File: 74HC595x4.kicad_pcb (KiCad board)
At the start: 2 copper layers, 45 parts, among them P1 CONN_01X06, P2 CONN_02X08, P3 CONN_02X08, P4 CONN_02X08, P5 CONN_02X08, U1 74HC595, U2 74HC595, U3 74HC595, U4 74HC595

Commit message: расставлено по сетке, исправлены ошибки
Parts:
- added C1: C, Capacitors_SMD:C_0805_HandSoldering, F.Cu at (104.1, 88.6)
- added C2: C, Capacitors_SMD:C_0805_HandSoldering, F.Cu at (104.1, 113.0)
- added C3: C, Capacitors_SMD:C_0805_HandSoldering, F.Cu at (132.1, 88.6)
- added C4: C, Capacitors_SMD:C_0805_HandSoldering, F.Cu at (132.1, 113.0)
- moved R27 51.3 mm to (139.7, 105.4)
- moved R29 51.3 mm to (147.3, 105.4)
- moved R17 51.3 mm to (121.9, 105.4)
- moved R19 51.3 mm to (111.8, 105.4)
- moved R22 51.3 mm to (114.3, 105.4)
- moved R24 51.3 mm to (104.1, 105.4)
- moved R18 51.3 mm to (116.8, 105.4)
- moved R20 51.3 mm to (106.7, 105.4)
- moved R21 51.3 mm to (119.4, 105.4)
- moved R23 51.3 mm to (109.2, 105.4)
- moved R25 51.3 mm to (149.9, 105.4)
- moved R26 51.3 mm to (144.8, 105.4)
- moved R28 51.3 mm to (134.6, 105.4)
- moved R30 51.3 mm to (142.2, 105.4)
- moved R31 51.3 mm to (137.2, 105.4)
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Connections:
- U2 pad 11: /74HC595_1/DS -> /74HC595_1/SH_CP
- U2 pad 12: /74HC595_1/SH_CP -> /74HC595_1/ST_CP
- U3 pad 11: /74HC595_1/DS -> /74HC595_1/SH_CP
- U3 pad 12: /74HC595_1/SH_CP -> /74HC595_1/ST_CP
- U4 pad 11: /74HC595_1/DS -> /74HC595_1/SH_CP
- U4 pad 12: /74HC595_1/SH_CP -> /74HC595_1/ST_CP
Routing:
- net GND: track 205.5 -> 19.9 mm, vias 0 -> 10
- net VCC: track 0.00 -> 131.4 mm, vias 0 -> 6
- net /74HC595_1/ST_CP: track 0.00 -> 107.9 mm, vias 0 -> 2
- net /74HC595_1/SH_CP: track 0.00 -> 99.8 mm, vias 0 -> 6
- net /74HC595_3/DS: track 0.00 -> 42.6 mm, vias 0 -> 2
- net /74HC595_2/DS: track 0.00 -> 40.7 mm, vias 0 -> 2
- net /74HC595_4/DS: track 0.00 -> 40.0 mm
- net /74HC595_1/DS: track 0.00 -> 19.1 mm, vias 0 -> 1
- net Net-(R29-Pad2): track 7.12 -> 5.01 mm
- net Net-(R26-Pad2): track 6.00 -> 3.88 mm
- net Net-(R10-Pad2): track 5.85 -> 3.88 mm
- net Net-(R2-Pad2): track 5.81 -> 3.88 mm
- net Net-(R18-Pad2): track 5.78 -> 3.88 mm
- net Net-(R5-Pad2): track 6.49 -> 5.01 mm
- net Net-(R13-Pad2): track 6.53 -> 5.15 mm
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
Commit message: пред готовность. толстые питающие метрические размеры
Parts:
- moved REF** 3.47 mm to (96.0, 119.0)
- moved REF** 3.44 mm to (156.0, 119.0)
- moved REF** 1.07 mm to (96.0, 74.0)
- moved REF** 0.95 mm to (156.0, 74.0)
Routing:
- net /74HC595_4/~Q7: track 0.00 -> 49.5 mm, vias 0 -> 1
- net VCC: track 131.4 -> 139.7 mm, vias 6 -> 8
- net GND: track 19.9 -> 24.4 mm, vias 10 -> 9
- net /74HC595_1/SH_CP: track 99.8 -> 103.1 mm, vias 6 -> 5
- net /74HC595_4/DS: track 40.0 -> 41.3 mm
- net /74HC595_1/ST_CP: track 107.9 -> 106.9 mm
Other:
- board outline added: 70 x 55 mm
- net class power added: clearance 0.2, trace_width 0.5, via_dia 0.6, via_drill 0.4

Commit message: мелкие доделки переразвод
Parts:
- moved REF** 10.0 mm to (96.0, 84.0)
- moved REF** 10.0 mm to (156.0, 84.0)
- moved P1 5.36 mm to (96.0, 94.7)
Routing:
- net VCC: track 139.7 -> 145.2 mm
- net /74HC595_4/~Q7: track 49.5 -> 44.0 mm
- net /74HC595_3/DS: track 42.6 -> 47.5 mm
- net /74HC595_1/DS: track 19.1 -> 22.7 mm
- net GND: track 24.4 -> 21.2 mm, vias 9 -> 10
- net /74HC595_1/SH_CP: track 103.1 -> 105.4 mm, vias 5 -> 4
- net /74HC595_1/ST_CP: track 106.9 -> 105.0 mm, vias 2 -> 1
- net Net-(R17-Pad2): track 12.3 -> 14.1 mm
- net Net-(R1-Pad2): track 12.3 -> 13.7 mm
- net /74HC595_2/DS: track 40.7 -> 41.4 mm

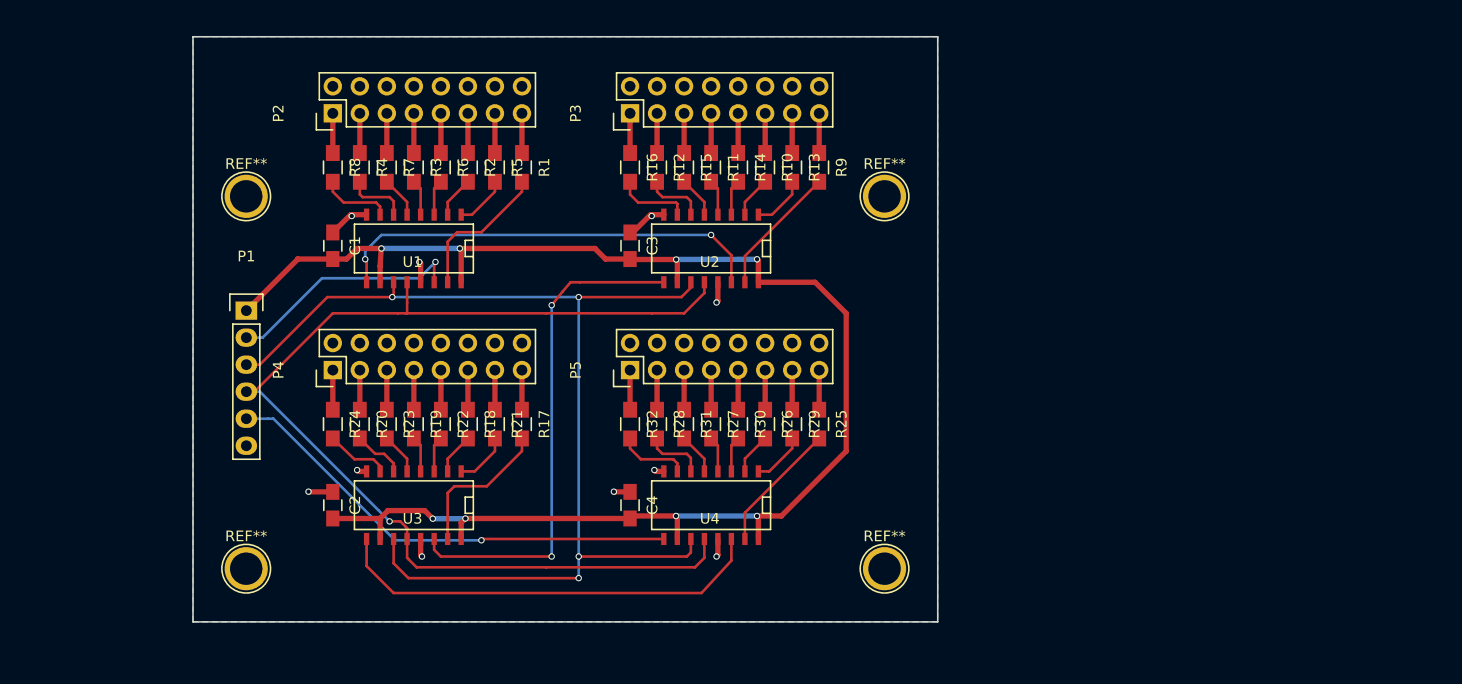
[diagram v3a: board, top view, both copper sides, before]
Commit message: изменен входной разъем
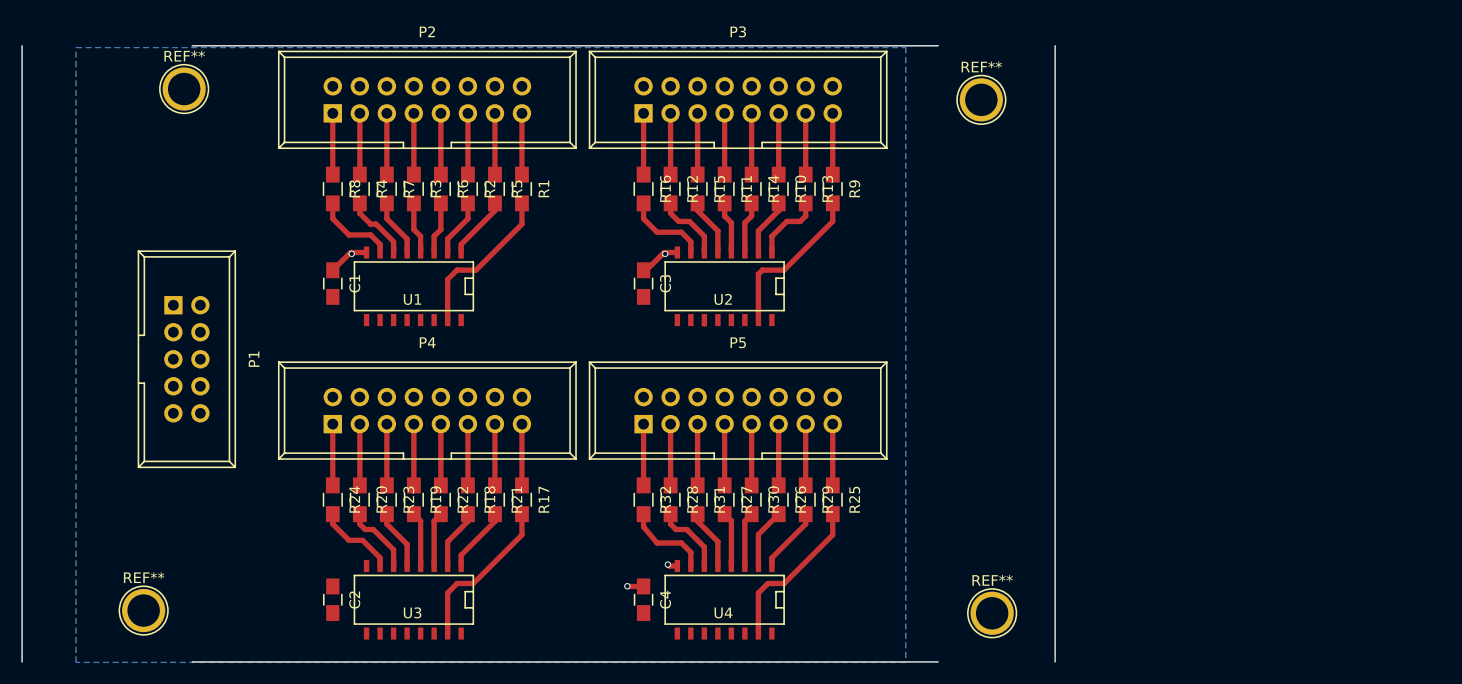
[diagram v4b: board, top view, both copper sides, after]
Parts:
- removed the REF** at (96.0, 119.0)
- removed the REF** at (96.0, 84.0)
- removed the REF** at (156.0, 119.0)
- removed the REF** at (156.0, 84.0)
- added REF**: 1pin, Connect:1pin, F.Cu at (165.1, 74.9)
- added REF**: 1pin, Connect:1pin, F.Cu at (166.1, 123.2)
- added REF**: 1pin, Connect:1pin, F.Cu at (90.2, 73.9)
- added REF**: 1pin, Connect:1pin, F.Cu at (86.4, 122.9)
- P1: value CONN_01X06 -> CONN_02X05; footprint Pin_Headers:Pin_Header_Straight_1x06 -> Connect:IDC_Header_Straight_10pins
- P2, P3, P4, P5: footprint Pin_Headers:Pin_Header_Straight_2x08 -> Connect:IDC_Header_Straight_16pins
- moved U4 8.98 mm to (141.0, 121.9)
- moved C4 8.98 mm to (133.3, 121.9)
- moved C2 8.89 mm to (104.1, 121.9)
- moved U3 8.89 mm to (111.8, 121.9)
- moved R26 7.22 mm to (146.1, 112.5)
- moved R27 7.22 mm to (141.0, 112.5)
- moved R29 7.22 mm to (148.6, 112.5)
- moved R31 7.22 mm to (138.4, 112.5)
- moved R25 7.22 mm to (151.1, 112.5)
- moved R28 7.22 mm to (135.9, 112.5)
- moved R30 7.22 mm to (143.5, 112.5)
- moved R32 7.22 mm to (133.3, 112.5)
- moved R17 7.11 mm to (121.9, 112.5)
- moved R18 7.11 mm to (116.8, 112.5)
- moved R19 7.11 mm to (111.8, 112.5)
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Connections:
- P1 pad 2: /74HC595_1/DS -> VCC
- P1 pad 3: /74HC595_1/SH_CP -> VCC
- P1 pad 4: /74HC595_1/ST_CP -> /74HC595_1/DS
- P1 pad 5: /74HC595_4/~Q7 -> GND
- P1 pad 6: GND -> /74HC595_1/SH_CP
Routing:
- net VCC: track 145.2 -> 0.77 mm, vias 8 -> 0
- net /74HC595_1/ST_CP: track 105.0 -> 0.00 mm, vias 1 -> 0
- net /74HC595_1/SH_CP: track 105.4 -> 0.51 mm, vias 4 -> 0
- net /74HC595_3/DS: track 47.5 -> 0.00 mm, vias 2 -> 0
- net /74HC595_4/~Q7: track 44.0 -> 0.00 mm, vias 1 -> 0
- net /74HC595_2/DS: track 41.4 -> 0.00 mm, vias 2 -> 0
- net /74HC595_4/DS: track 41.3 -> 0.00 mm
- net /74HC595_1/DS: track 22.7 -> 0.00 mm, vias 1 -> 0
- net GND: track 21.2 -> 10.6 mm, vias 10 -> 4
- net Net-(R9-Pad2): track 12.3 -> 15.1 mm
- net Net-(R25-Pad2): track 12.3 -> 15.0 mm
- net Net-(P3-Pad5): track 3.73 -> 5.84 mm
- net Net-(P5-Pad9): track 3.73 -> 5.76 mm
- net Net-(P5-Pad7): track 3.73 -> 5.76 mm
- net Net-(P5-Pad5): track 3.73 -> 5.76 mm
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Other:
- board size 70 x 55 mm -> 97.1 x 57.9 mm
